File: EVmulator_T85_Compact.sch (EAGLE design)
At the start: 24 parts, among them Q2 DMN3404L-7, U1 ATTINY85V

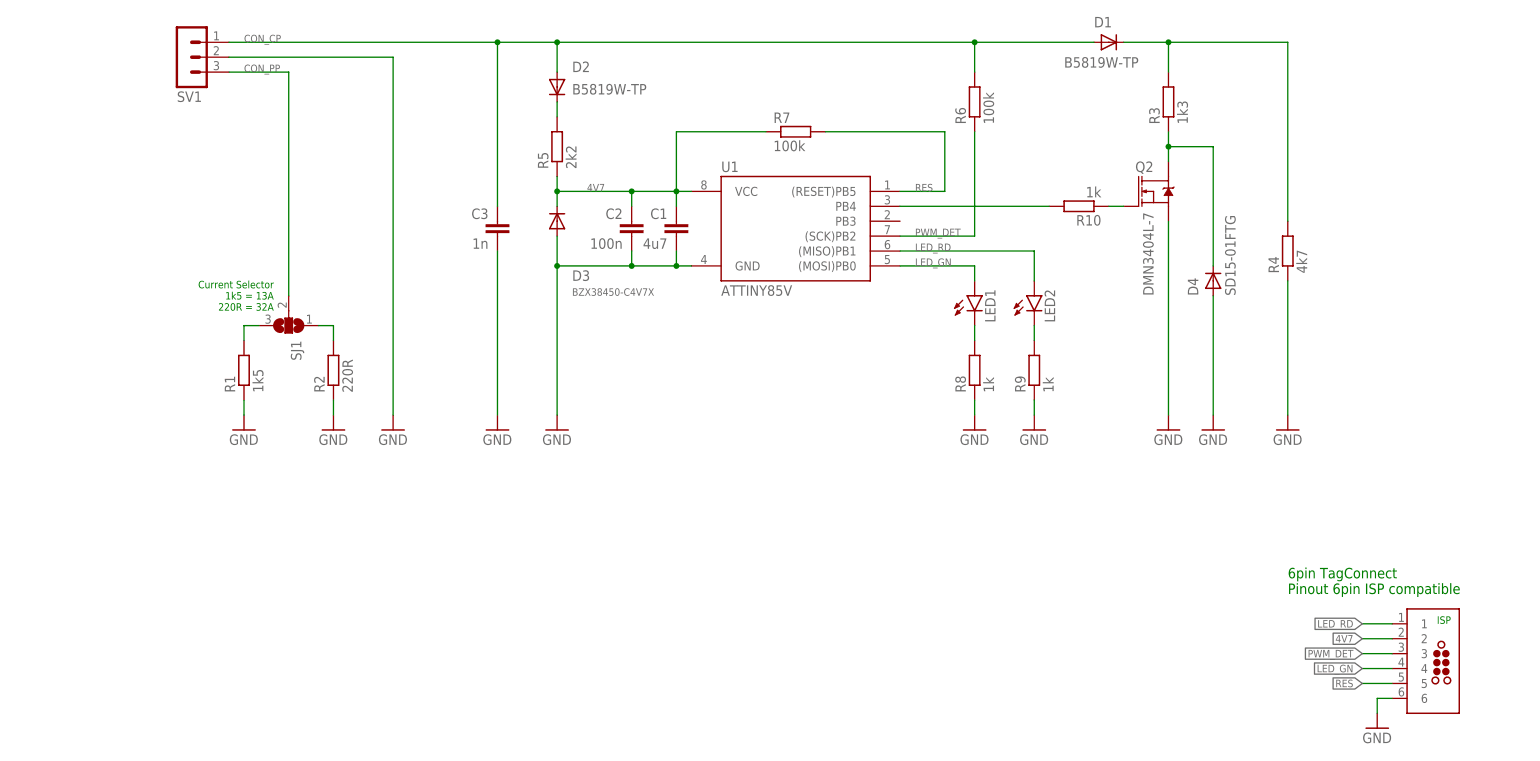
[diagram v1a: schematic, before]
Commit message: * moved prototype board to deprecated (will not be maintained in the future= * added connection drawing to schematic, updated output
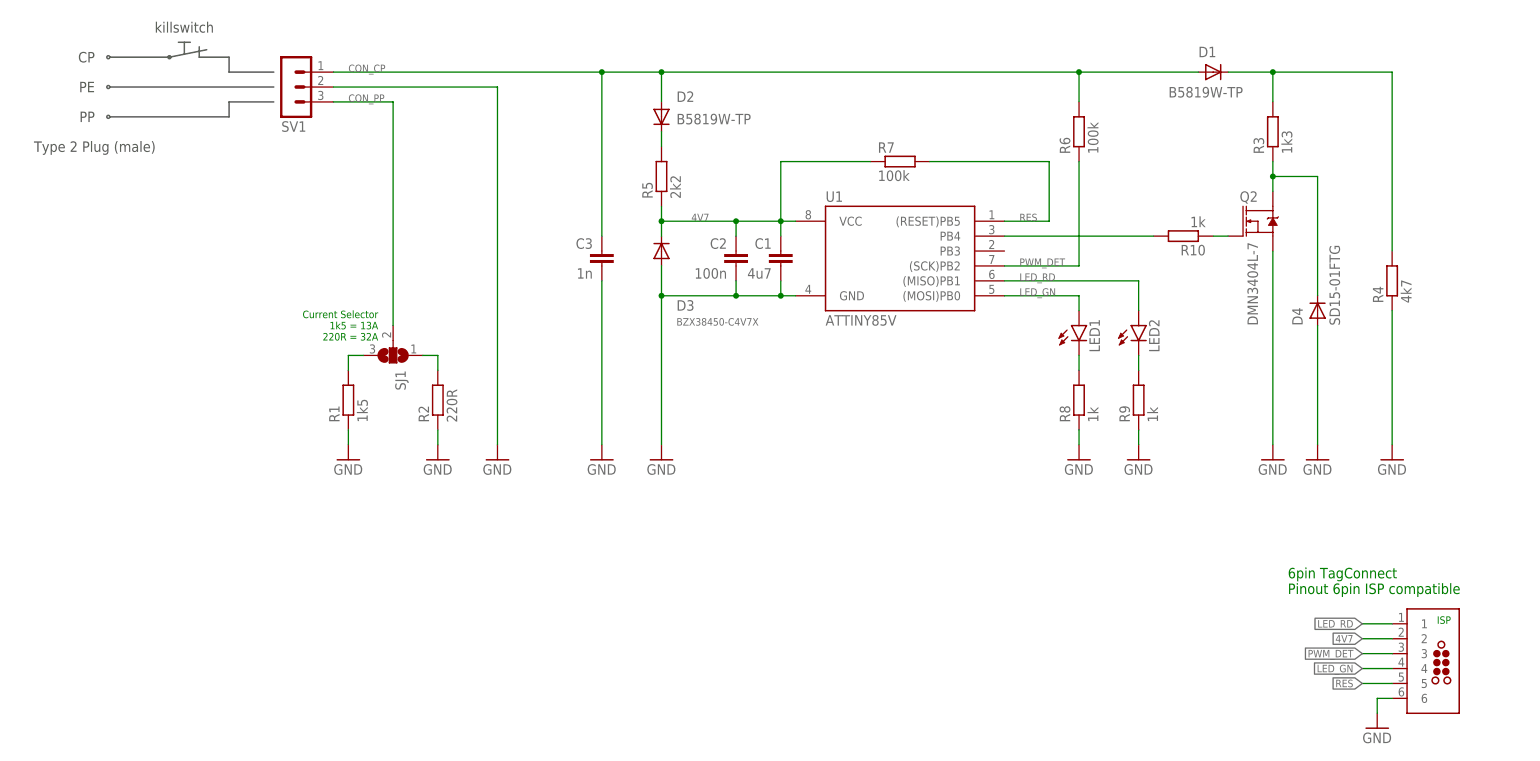
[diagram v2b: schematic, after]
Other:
- note added: "CP"
- note added: "PE"
- note added: "PP"
- note added: "Type 2 Plug (male)"
- note added: "killswitch"
- moved on the sheet: C1, C2, C3, D1, D2, D3, D4, LED1, LED2, Q2, R1, R10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
